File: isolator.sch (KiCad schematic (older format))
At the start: 3 parts, among them U1 Si8660

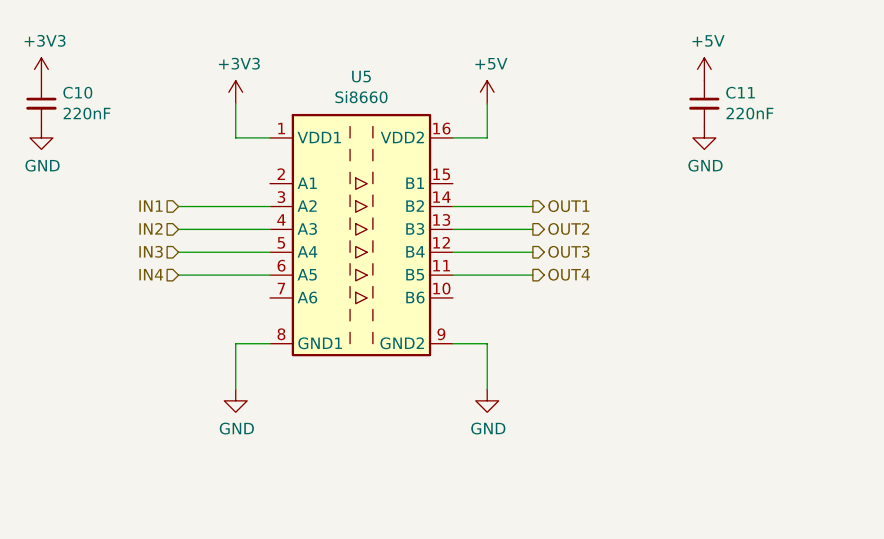
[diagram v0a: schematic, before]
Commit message: Updated RJ45 symbol and corresponding signal names
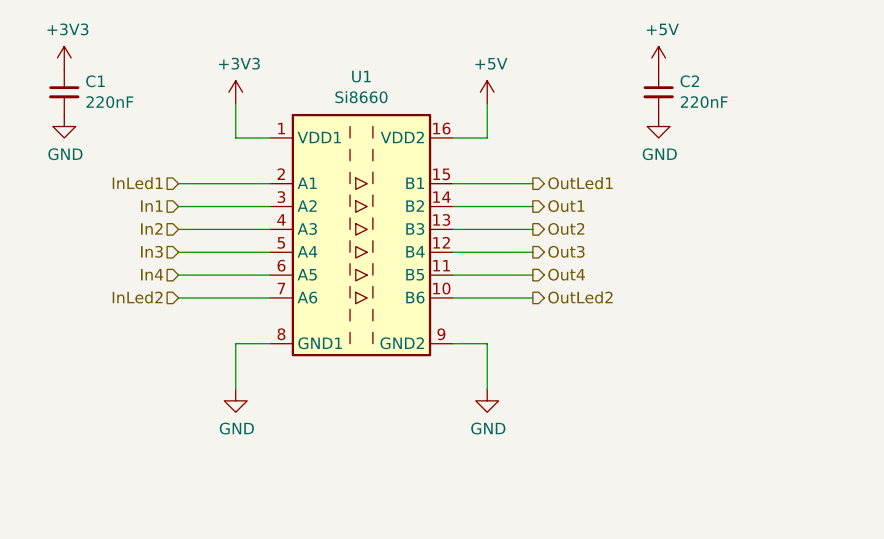
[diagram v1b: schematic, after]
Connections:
- net OutLed2: now reaches U1.10 (B6)
- net OutLed1: now reaches U1.15 (B1)
- net InLed1: now reaches U1.2 (A1)
- net InLed2: now reaches U1.7 (A6)
- net IN1 renamed In1
- net IN2 renamed In2
- net IN3 renamed In3
- net IN4 renamed In4
- net OUT1 renamed Out1
- net OUT2 renamed Out2
- net OUT3 renamed Out3
- net OUT4 renamed Out4
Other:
- moved on the sheet: C1, C2
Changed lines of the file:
@@
 $Descr A4 11693 8268
 encoding utf-8
-Sheet 6 11
+Sheet 3 11
 Title ""
 Date ""
@@
 $EndDescr
 Text HLabel 4400 3400 0    50   Input ~ 0
-IN1
+In1
 Text HLabel 4400 3500 0    50   Input ~ 0
-IN2
+In2
 Text HLabel 4400 3600 0    50   Input ~ 0
-IN3
+In3
 Text HLabel 4400 3700 0    50   Input ~ 0
-IN4
+In4
 Text HLabel 5950 3400 2    50   Output ~ 0
-OUT1
+Out1
 Text HLabel 5950 3500 2    50   Output ~ 0
-OUT2
+Out2
 Text HLabel 5950 3600 2    50   Output ~ 0
-OUT3
+Out3
 Text HLabel 5950 3700 2    50   Output ~ 0
-OUT4
+Out4
 $Comp
 L power:+3V3 #PWR07
@@
 AR Path="/5BCC7A96/5BCC7DB8" Ref="#PWR020"  Part="1"
 AR Path="/5BCC8BB7/5BCC7DB8" Ref="#PWR036"  Part="1"
-F 0 "#PWR036" H 4650 2800 50  0001 C CNN
+F 0 "#PWR07" H 4650 2800 50  0001 C CNN
 F 1 "+3V3" H 4665 3123 50  0000 C CNN
 F 2 "" H 4650 2950 50  0001 C CNN
@@
 AR Path="/5BCC7A96/5BCC7E07" Ref="#PWR022"  Part="1"
 AR Path="/5BCC8BB7/5BCC7E07" Ref="#PWR038"  Part="1"
-F 0 "#PWR038" H 5750 2800 50  0001 C CNN
+F 0 "#PWR09" H 5750 2800 50  0001 C CNN
 F 1 "+5V" H 5765 3123 50  0000 C CNN
 F 2 "" H 5750 2950 50  0001 C CNN
@@
 L power:+3V3 #PWR05
 U 1 1 5BCCF224
-P 3800 2850
+P 3900 2800
 AR Path="/5BCC578B/5BCCF224" Ref="#PWR05"  Part="1"
 AR Path="/5BCC79AE/5BCCF224" Ref="#PWR026"  Part="1"
 AR Path="/5BCC7A96/5BCCF224" Ref="#PWR018"  Part="1"
 AR Path="/5BCC8BB7/5BCCF224" Ref="#PWR034"  Part="1"
-F 0 "#PWR034" H 3800 2700 50  0001 C CNN
-F 1 "+3V3" H 3815 3023 50  0000 C CNN
-F 2 "" H 3800 2850 50  0001 C CNN
-F 3 "" H 3800 2850 50  0001 C CNN
-	1    3800 2850
+F 0 "#PWR05" H 3900 2650 50  0001 C CNN
+F 1 "+3V3" H 3915 2973 50  0000 C CNN
+F 2 "" H 3900 2800 50  0001 C CNN
+F 3 "" H 3900 2800 50  0001 C CNN
+	1    3900 2800
 	1    0    0    -1
 $EndComp
@@
 L Device:C_Small C1
 U 1 1 5BCCF242
-P 3800 2950
+P 3900 2900
 AR Path="/5BCC578B/5BCCF242" Ref="C1"  Part="1"
 AR Path="/5BCC79AE/5BCCF242" Ref="C8"  Part="1"
 AR Path="/5BCC7A96/5BCCF242" Ref="C6"  Part="1"
 AR Path="/5BCC8BB7/5BCCF242" Ref="C10"  Part="1"
-F 0 "C10" H 3892 2996 50  0000 L CNN
-F 1 "220nF" H 3892 2905 50  0000 L CNN
-F 2 "Capacitor_SMD:C_0805_2012Metric_Pad1.15x1.40mm_HandSolder" H 3800 2950 50  0001 C CNN
-F 3 "~" H 3800 2950 50  0001 C CNN
-	1    3800 2950
+F 0 "C1" H 3992 2946 50  0000 L CNN
+F 1 "220nF" H 3992 2855 50  0000 L CNN
+F 2 "Capacitor_SMD:C_0805_2012Metric_Pad1.15x1.40mm_HandSolder" H 3900 2900 50  0001 C CNN
+F 3 "~" H 3900 2900 50  0001 C CNN
+	1    3900 2900
 	1    0    0    -1
 $EndComp
@@
 L Device:C_Small C2
 U 1 1 5BCCF2B7
-P 6700 2950
+P 6500 2900
 AR Path="/5BCC578B/5BCCF2B7" Ref="C2"  Part="1"
 AR Path="/5BCC79AE/5BCCF2B7" Ref="C9"  Part="1"
 AR Path="/5BCC7A96/5BCCF2B7" Ref="C7"  Part="1"
 AR Path="/5BCC8BB7/5BCCF2B7" Ref="C11"  Part="1"
-F 0 "C11" H 6792 2996 50  0000 L CNN
-F 1 "220nF" H 6792 2905 50  0000 L CNN
-F 2 "Capacitor_SMD:C_0805_2012Metric_Pad1.15x1.40mm_HandSolder" H 6700 2950 50  0001 C CNN
-F 3 "~" H 6700 2950 50  0001 C CNN
-	1    6700 2950
+F 0 "C2" H 6592 2946 50  0000 L CNN
+F 1 "220nF" H 6592 2855 50  0000 L CNN
+F 2 "Capacitor_SMD:C_0805_2012Metric_Pad1.15x1.40mm_HandSolder" H 6500 2900 50  0001 C CNN
+F 3 "~" H 6500 2900 50  0001 C CNN
+	1    6500 2900
 	1    0    0    -1
 $EndComp
@@
 L power:+5V #PWR011
 U 1 1 5BCCF324
-P 6700 2850
+P 6500 2800
 AR Path="/5BCC578B/5BCCF324" Ref="#PWR011"  Part="1"
 AR Path="/5BCC79AE/5BCCF324" Ref="#PWR032"  Part="1"
 AR Path="/5BCC7A96/5BCCF324" Ref="#PWR024"  Part="1"
 AR Path="/5BCC8BB7/5BCCF324" Ref="#PWR040"  Part="1"
-F 0 "#PWR040" H 6700 2700 50  0001 C CNN
-F 1 "+5V" H 6715 3023 50  0000 C CNN
-F 2 "" H 6700 2850 50  0001 C CNN
-F 3 "" H 6700 2850 50  0001 C CNN
-	1    6700 2850
+F 0 "#PWR011" H 6500 2650 50  0001 C CNN
+F 1 "+5V" H 6515 2973 50  0000 C CNN
+F 2 "" H 6500 2800 50  0001 C CNN
+F 3 "" H 6500 2800 50  0001 C CNN
+	1    6500 2800
 	1    0    0    -1
 $EndComp
@@
 L power:GND #PWR06
 U 1 1 5BCF7281
-P 3800 3050
+P 3900 3000
 AR Path="/5BCC578B/5BCF7281" Ref="#PWR06"  Part="1"
 AR Path="/5BCC7A96/5BCF7281" Ref="#PWR019"  Part="1"
 AR Path="/5BCC79AE/5BCF7281" Ref="#PWR027"  Part="1"
 AR Path="/5BCC8BB7/5BCF7281" Ref="#PWR035"  Part="1"
-F 0 "#PWR035" H 3800 2800 50  0001 C CNN
-F 1 "GND" H 3805 2877 50  0000 C CNN
-F 2 "" H 3800 3050 50  0001 C CNN
-F 3 "" H 3800 3050 50  0001 C CNN
-	1    3800 3050
+F 0 "#PWR06" H 3900 2750 50  0001 C CNN
+F 1 "GND" H 3905 2827 50  0000 C CNN
+F 2 "" H 3900 3000 50  0001 C CNN
+F 3 "" H 3900 3000 50  0001 C CNN
+	1    3900 3000
 	1    0    0    -1
 $EndComp
@@
 AR Path="/5BCC79AE/5BCF7299" Ref="#PWR029"  Part="1"
 AR Path="/5BCC8BB7/5BCF7299" Ref="#PWR037"  Part="1"
-F 0 "#PWR037" H 4650 3950 50  0001 C CNN
+F 0 "#PWR08" H 4650 3950 50  0001 C CNN
 F 1 "GND" H 4655 4027 50  0000 C CNN
 F 2 "" H 4650 4200 50  0001 C CNN
@@
 AR Path="/5BCC79AE/5BCF72AA" Ref="#PWR031"  Part="1"
 AR Path="/5BCC8BB7/5BCF72AA" Ref="#PWR039"  Part="1"
-F 0 "#PWR039" H 5750 3950 50  0001 C CNN
+F 0 "#PWR010" H 5750 3950 50  0001 C CNN
 F 1 "GND" H 5755 4027 50  0000 C CNN
 F 2 "" H 5750 4200 50  0001 C CNN
@@
 L power:GND #PWR012
 U 1 1 5BCF72BB
-P 6700 3050
+P 6500 3000
 AR Path="/5BCC578B/5BCF72BB" Ref="#PWR012"  Part="1"
 AR Path="/5BCC7A96/5BCF72BB" Ref="#PWR025"  Part="1"
 AR Path="/5BCC79AE/5BCF72BB" Ref="#PWR033"  Part="1"
 AR Path="/5BCC8BB7/5BCF72BB" Ref="#PWR041"  Part="1"
-F 0 "#PWR041" H 6700 2800 50  0001 C CNN
-F 1 "GND" H 6705 2877 50  0000 C CNN
-F 2 "" H 6700 3050 50  0001 C CNN
-F 3 "" H 6700 3050 50  0001 C CNN
-	1    6700 3050
+F 0 "#PWR012" H 6500 2750 50  0001 C CNN
+F 1 "GND" H 6505 2827 50  0000 C CNN
+F 2 "" H 6500 3000 50  0001 C CNN
+F 3 "" H 6500 3000 50  0001 C CNN
+	1    6500 3000
 	1    0    0    -1
 $EndComp
@@
 AR Path="/5BCC79AE/5BE0D51C" Ref="U4"  Part="1"
 AR Path="/5BCC8BB7/5BE0D51C" Ref="U5"  Part="1"
-F 0 "U5" H 5200 4167 50  0000 C CNN
+F 0 "U1" H 5200 4167 50  0000 C CNN
 F 1 "Si8660" H 5200 4076 50  0000 C CNN
 F 2 "Package_SO:SOIC-16_3.9x9.9mm_P1.27mm" H 5200 2850 50  0001 C CIN
@@
 	1    0    0    -1
 $EndComp
+Text HLabel 4400 3300 0    50   Input ~ 0
+InLed1
+Wire Wire Line
+	4400 3300 4800 3300
+Text HLabel 5950 3300 2    50   Output ~ 0
+OutLed1
+Text HLabel 5950 3800 2    50   Output ~ 0
+OutLed2
+Text HLabel 4400 3800 0    50   Input ~ 0
+InLed2
+Wire Wire Line
+	4400 3800 4800 3800
+Wire Wire Line
+	5600 3800 5950 3800
+Wire Wire Line
+	5600 3300 5950 3300
 $EndSCHEMATC

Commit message: Began redesigning with Si8660
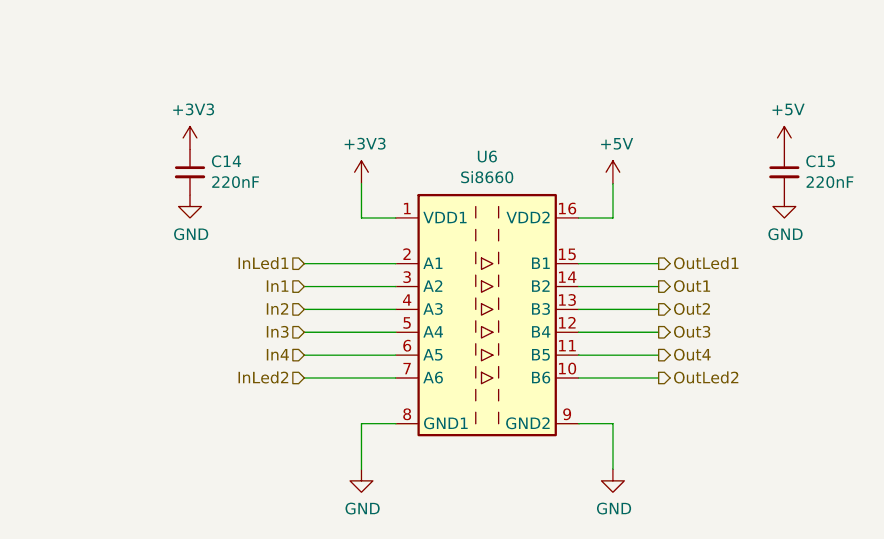
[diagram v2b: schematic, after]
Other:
- moved on the sheet: C14, C15, U6

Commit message: Finished layout with 4x Si8660
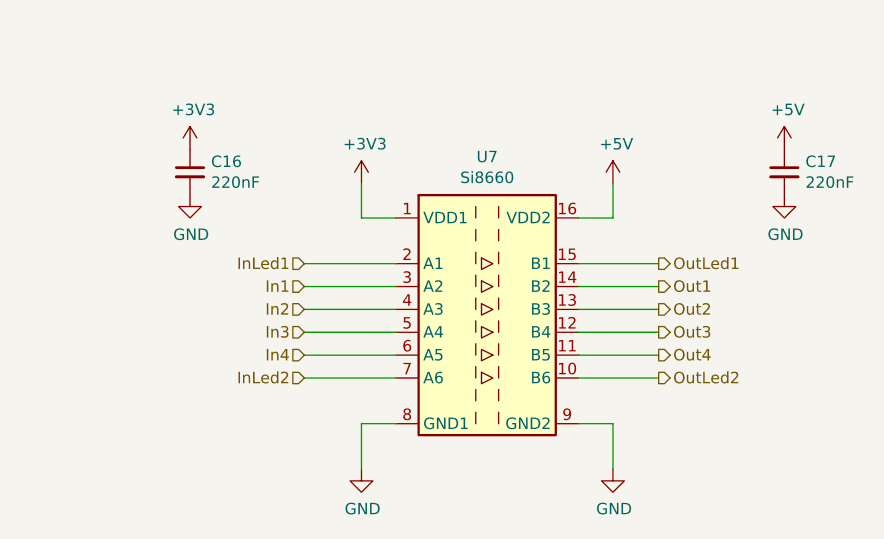
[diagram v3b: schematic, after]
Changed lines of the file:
@@
 $Descr A4 11693 8268
 encoding utf-8
-Sheet 9 11
+Sheet 4 11
 Title ""
 Date ""
@@
 AR Path="/5BCC7A96/5BCCF242" Ref="C16"  Part="1"
 AR Path="/5BCC8BB7/5BCCF242" Ref="C14"  Part="1"
-F 0 "C14" H 4542 3296 50  0000 L CNN
+F 0 "C16" H 4542 3296 50  0000 L CNN
 F 1 "220nF" H 4542 3205 50  0000 L CNN
 F 2 "Capacitor_SMD:C_0805_2012Metric_Pad1.15x1.40mm_HandSolder" H 4450 3250 50  0001 C CNN
@@
 AR Path="/5BCC7A96/5BCCF2B7" Ref="C17"  Part="1"
 AR Path="/5BCC8BB7/5BCCF2B7" Ref="C15"  Part="1"
-F 0 "C15" H 7142 3296 50  0000 L CNN
+F 0 "C17" H 7142 3296 50  0000 L CNN
 F 1 "220nF" H 7142 3205 50  0000 L CNN
 F 2 "Capacitor_SMD:C_0805_2012Metric_Pad1.15x1.40mm_HandSolder" H 7050 3250 50  0001 C CNN
@@
 AR Path="/5BCC79AE/5BE0D51C" Ref="U5"  Part="1"
 AR Path="/5BCC8BB7/5BE0D51C" Ref="U6"  Part="1"
-F 0 "U6" H 5750 4517 50  0000 C CNN
+F 0 "U7" H 5750 4517 50  0000 C CNN
 F 1 "Si8660" H 5750 4426 50  0000 C CNN
 F 2 "Package_SO:SOIC-16_3.9x9.9mm_P1.27mm" H 5750 3200 50  0001 C CIN
